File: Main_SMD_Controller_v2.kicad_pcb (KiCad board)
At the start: 4 copper layers, 100 x 100 mm, 184 parts, among them J101 ETB43034G000Z, J102 ETB43034G000Z, J103 B2P3-VH-3.3(LF)(SN), J104 PH-1X3SG, J105 PCB-20, J106 B2B-XH-A, J107 PCB-20, J108 PH-1X2SG, J109 PCB-20, J110 PCB-20, J111 B2B-XH-A, J112 PH-1X3SG, J301 BH-14SG, J302 PH-2x3SG, P101 Eoshi-chan_Silk, P102 Serial_QR, Q201 2SC1815, Q202 2SD1415A, Q203 TTB1020B, Q204 2SD1415A, Q205 TTB1020B, Q301 2N7002K, Q302 2N7002K, Q303 BSS84, Q304 2N7002K, Q305 2N7002K, U101 XC6201P332MR-G, U102 XC6902N331MR-G, U103 TC4066BP, U104 ADA4510-2ARZ, U105 MCP1501-20E/CHY, U106 LT1167CN8, U107 NJU7098A, U201 ADA4522-1ARZ, U202 KIA75S358F, U301 74LCX541FT, U302 SLG46826G, U303 PCA9515AD, U304 MCP4726A0T-ECH, U305 MCP3424T-ESL, U306 MCP9701A-E_TO

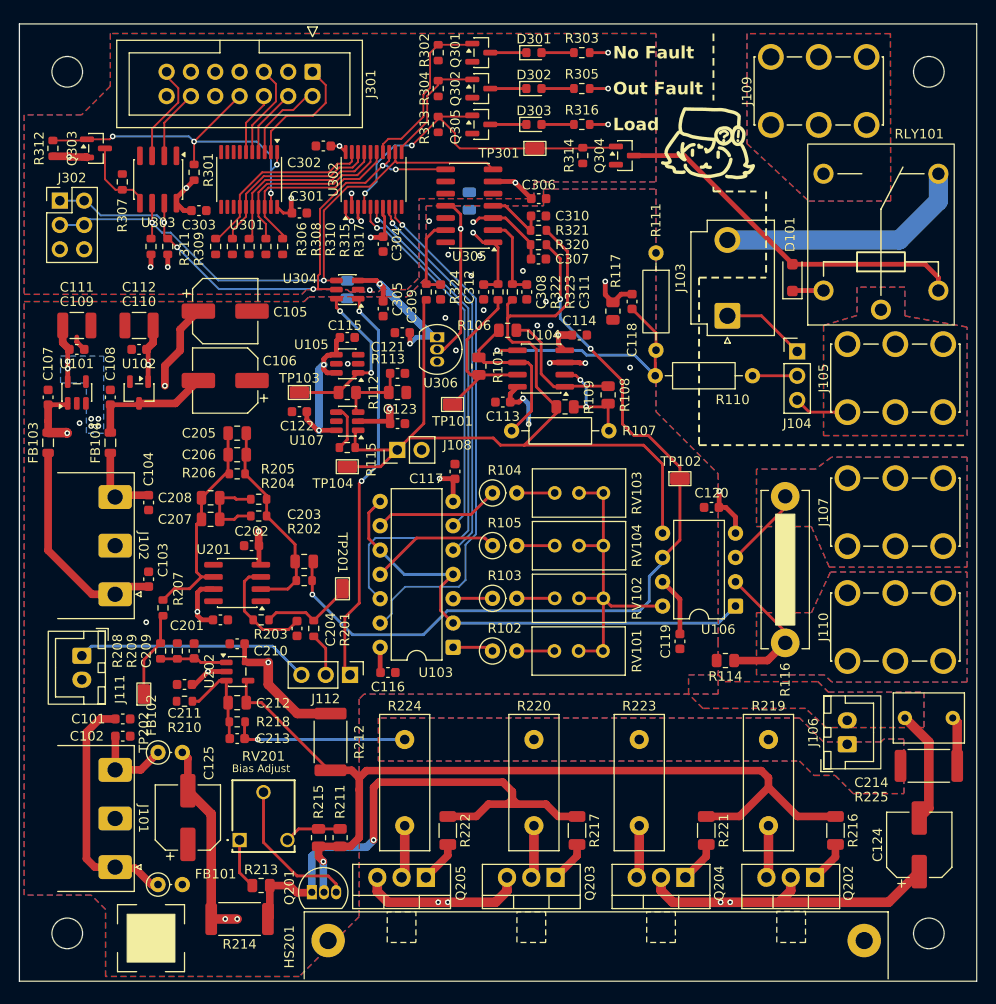
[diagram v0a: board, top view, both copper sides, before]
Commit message: アノテーションリセット 余計なもんも消す
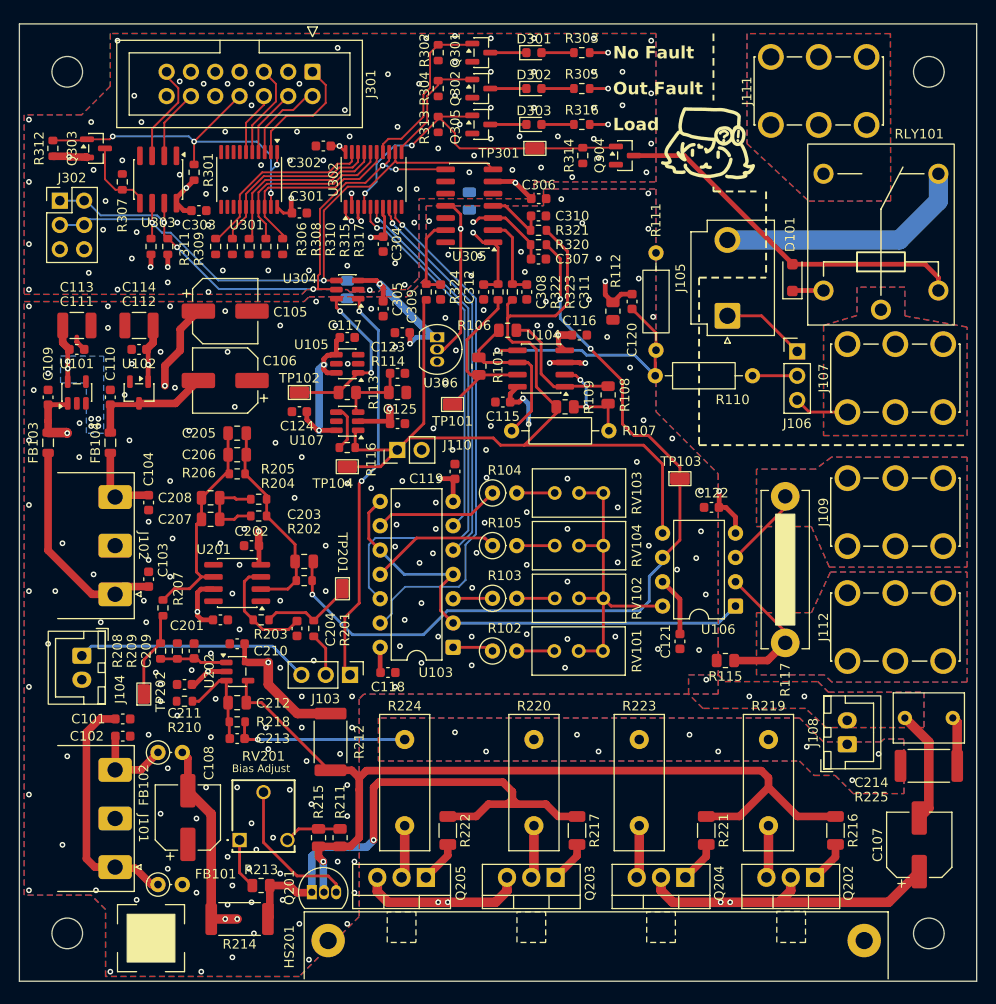
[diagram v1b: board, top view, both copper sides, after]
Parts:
- renumbered C124 to C107, C125 to C108, C107 to C109, C108 to C110, C109 to C111, C110 to C112, C111 to C113, C112 to C114, C113 to C115, C114 to C116, C115 to C117, C116 to C118, C117 to C119, C118 to C120, C119 to C121, C120 to C122, C121 to C123, C122 to C124, C123 to C125, J112 to J103, J111 to J104, J103 to J105, J104 to J106, J105 to J107, J106 to J108, J107 to J109, J108 to J110, J109 to J111, J110 to J112, R117 to R112, R112 to R113, R113 to R114, R114 to R115, R115 to R116, R116 to R117, TP103 to TP102, TP102 to TP103
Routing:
- net GNDD: vias 1 -> 81
- net GND: vias 15 -> 180
- net /MOS_G: vias 1 -> 10

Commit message: 完成
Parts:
- removed P102: Serial_QR, JLCPCB_Serial:Serial_QR_5x5
- P101: footprint Eoshi-chan_v2:Eoshi-chan-v2_10x10 -> Eoshi-chan_v2:Eoshi-chan-v2_7x7
- moved P101 4.45 mm to (119.2, 66.0), turned to 90 degrees
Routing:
- net GNDA: track 121.2 -> 116.5 mm
- net /MOS_S: track 8.53 -> 9.98 mm
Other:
- board text added: "-←"
- board text added: "2026-05-27"
- board text added: "B/G"
- board text added: "BIAS ADJ"
- board text added: "C/D"
- board text added: "E/S"
- board text added: "EXT"
- board text added: "EXT REF IN"
- board text added: "Electronic Load A-CONT v2.1"
- board text added: "GNDD"
- board text added: "IN+"
- board text added: "IN-"
- board text added: "INT"
- board text added: "SCL"
- board text added: "SDA"
- board text added: "V_{IN}"
- board text added: "V_{OFS}=0"
- board text added: "V_{SENS}"
- board text added: "±5V"
- board text added: "±5V (BJT) ±12V(MOS)"
- board text added: "→+"
- board text removed: "Bias Adjust"

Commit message: できたかも
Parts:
- moved C101 19.4 mm to (60.8, 142.0)
- moved C124 2.05 mm to (78.8, 92.5)
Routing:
- net Net-(J101-Pin_1): track 25.4 -> 9.16 mm
- net -3V3: track 128.8 -> 130.0 mm
- net +3V3: track 344.7 -> 343.9 mm
- net GND: vias 180 -> 184

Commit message: 現状確定
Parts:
- removed J103: PH-1X3SG, Connector_PinHeader_2.54mm:PinHeader_1x03_P2.54mm_Vertical
- removed J104: B2B-XH-A, Connector_JST:JST_XH_B2B-XH-A_1x02_P2.50mm_Vertical
- added J303: PH-1X3SG, Connector_PinHeader_2.54mm:PinHeader_1x03_P2.54mm_Vertical, F.Cu at (84.5, 118.0)
- added J304: B2B-XH-A, Connector_JST:JST_XH_B2B-XH-A_1x02_P2.50mm_Vertical, F.Cu at (56.5, 116.0)
- C212: value 1000p -> 1000p(FL)
- J105: value B2P3-VH-3.3(LF)(SN) -> B2P3-VH-3.3
- R116: value 100 -> 200
- U106: value LT1167CN8 -> AD623ANZ
- turned R112 to 90 degrees
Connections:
- R112 pad 1: GNDA -> GND
- R112 pad 2: GND -> GNDA
- U304 pad 1: /Interface/rt -> Net-(J303-Pin_1)
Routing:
- net Net-(J303-Pin_1): track 0.00 -> 41.8 mm, vias 0 -> 2
- net /Interface/rt: track 41.8 -> 0.00 mm, vias 2 -> 0
- net Net-(J303-Pin_3): track 0.00 -> 24.6 mm
- net Net-(J103-Pin_3): track 24.6 -> 0.00 mm
